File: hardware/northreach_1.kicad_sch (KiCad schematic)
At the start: 0 parts

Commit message: schematic: usb-c port section
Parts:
- added J1: USB_C_Receptacle, Connector_USB:USB_C_Receptacle_Amphenol_12401610E4-2A, symbol Connector:USB_C_Receptacle
- added R1, R2: 5.1k, Resistor_SMD:R_0805_2012Metric, symbol Device:R
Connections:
- new net: J1.A5 (CC1), R1.1
- new net: J1.B5 (CC2), R2.1
- new net GND: J1.A1 (GND), J1.A12 (GND), J1.B1 (GND), J1.B12 (GND), J1.S1 (SHIELD), R1.2, R2.2
- new net USB_D_NEGATIVE: J1.A7 (D-), J1.B7 (D-)
- new net USB_D_POSITIVE: J1.A6 (D+), J1.B6 (D+)
- new net VBUS: J1.A4 (VBUS), J1.A9 (VBUS), J1.B4 (VBUS), J1.B9 (VBUS)
- no-connect marks 0 -> 10
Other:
- note added: "USB-C Port"

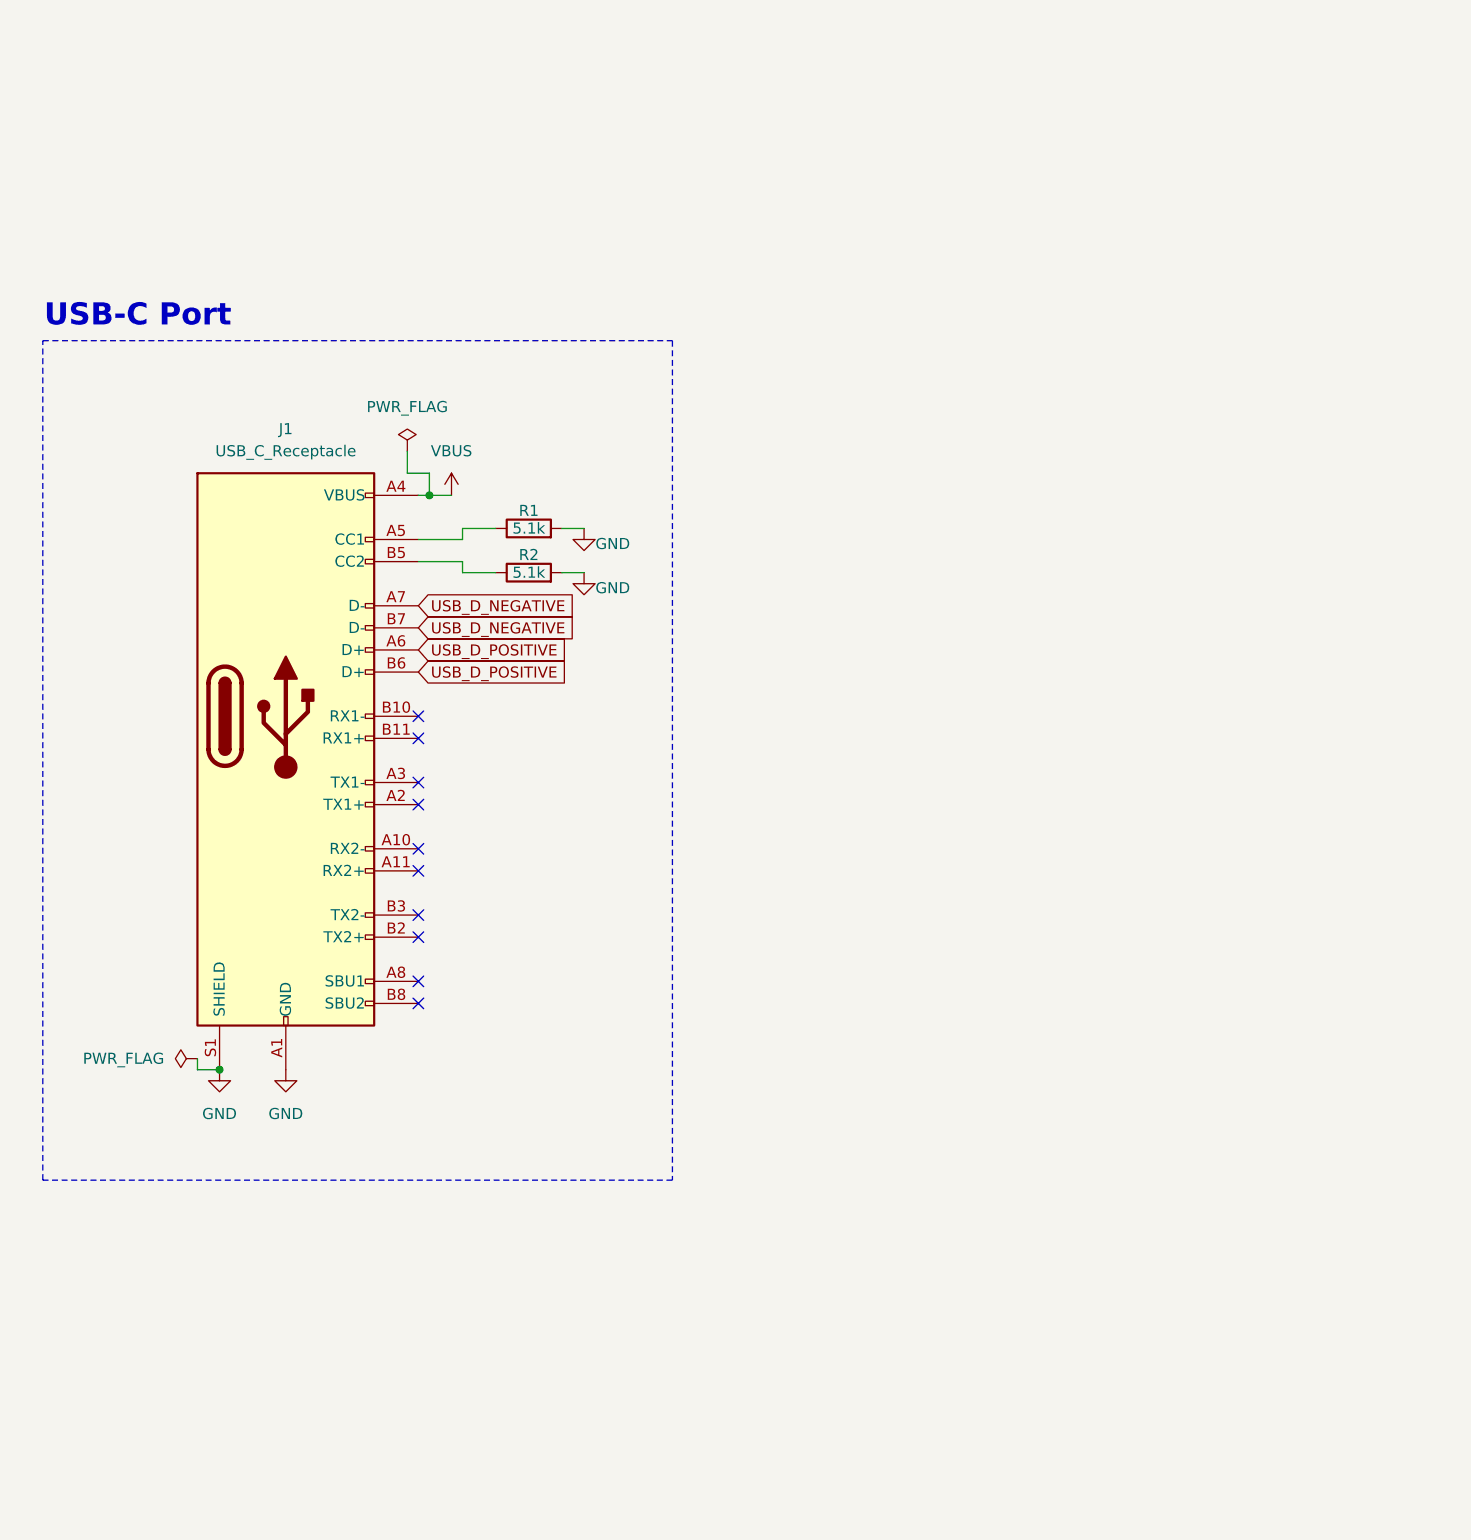
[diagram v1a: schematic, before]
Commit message: schematic: add voltage regulator
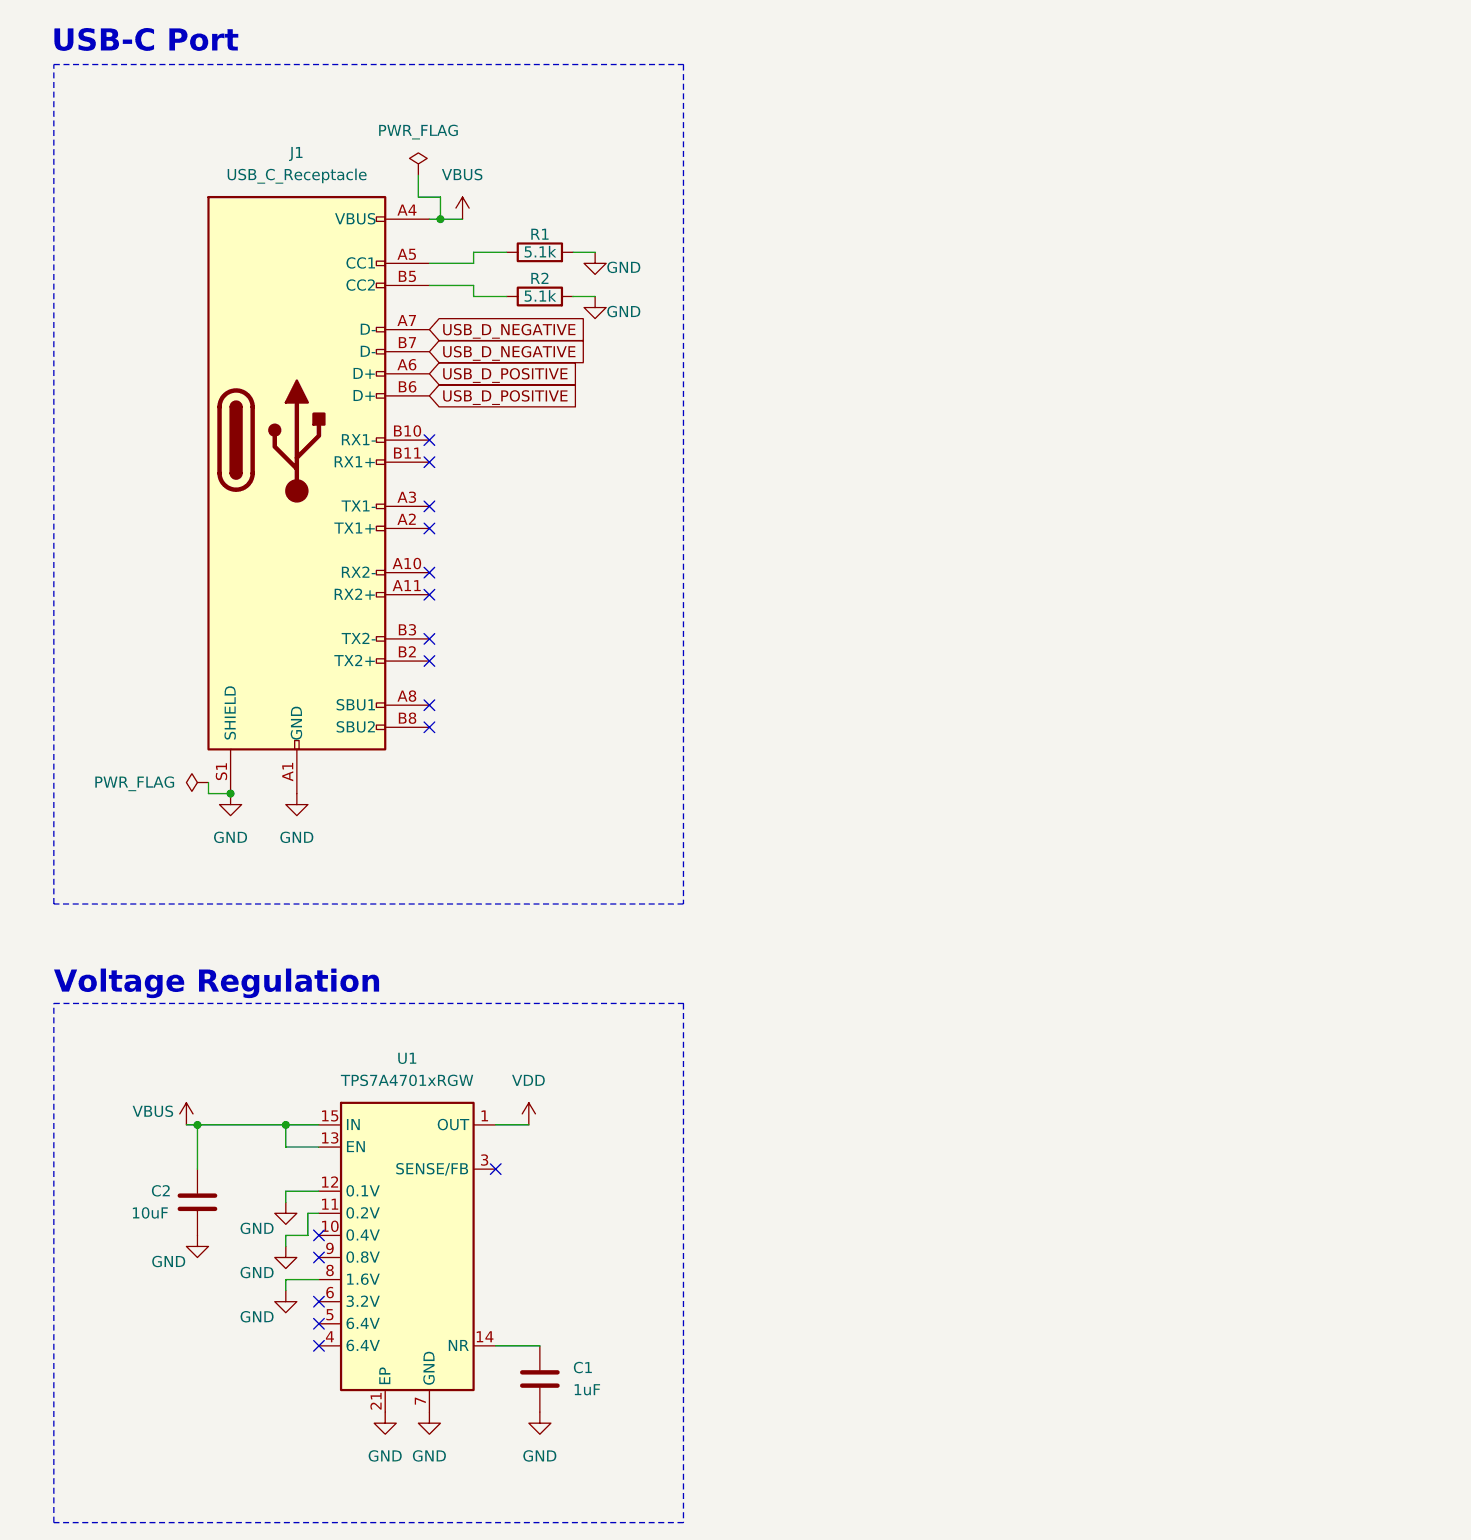
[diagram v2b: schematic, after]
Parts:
- added C1: 1uF, Capacitor_SMD:C_0805_2012Metric, symbol Device:C
- added C2: 10uF, Capacitor_SMD:C_0805_2012Metric, symbol Device:C
- added U1: TPS7A4701xRGW, Package_DFN_QFN:Texas_RGW0020A_VQFN-20-1EP_5x5mm_P0.65mm_EP3.15x3.15mm_ThermalVias, symbol Regulator_Linear:TPS7A4701xRGW
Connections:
- net GND: now also C1.1, C2.1, U1.11 (0.2V), U1.12 (0.1V), U1.21 (EP), U1.7 (GND), U1.8 (1.6V)
- net VBUS: now also C2.2, U1.13 (EN), U1.15 (IN), U1.16 (IN)
- new net: C1.2, U1.14 (NR)
- new net VDD: U1.1 (OUT), U1.20 (OUT)
- no-connect marks 10 -> 16
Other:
- note added: "Voltage Regulation"
- moved on the sheet: J1, R1, R2

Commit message: schematic: add MCU, and bootselect and reset buttons
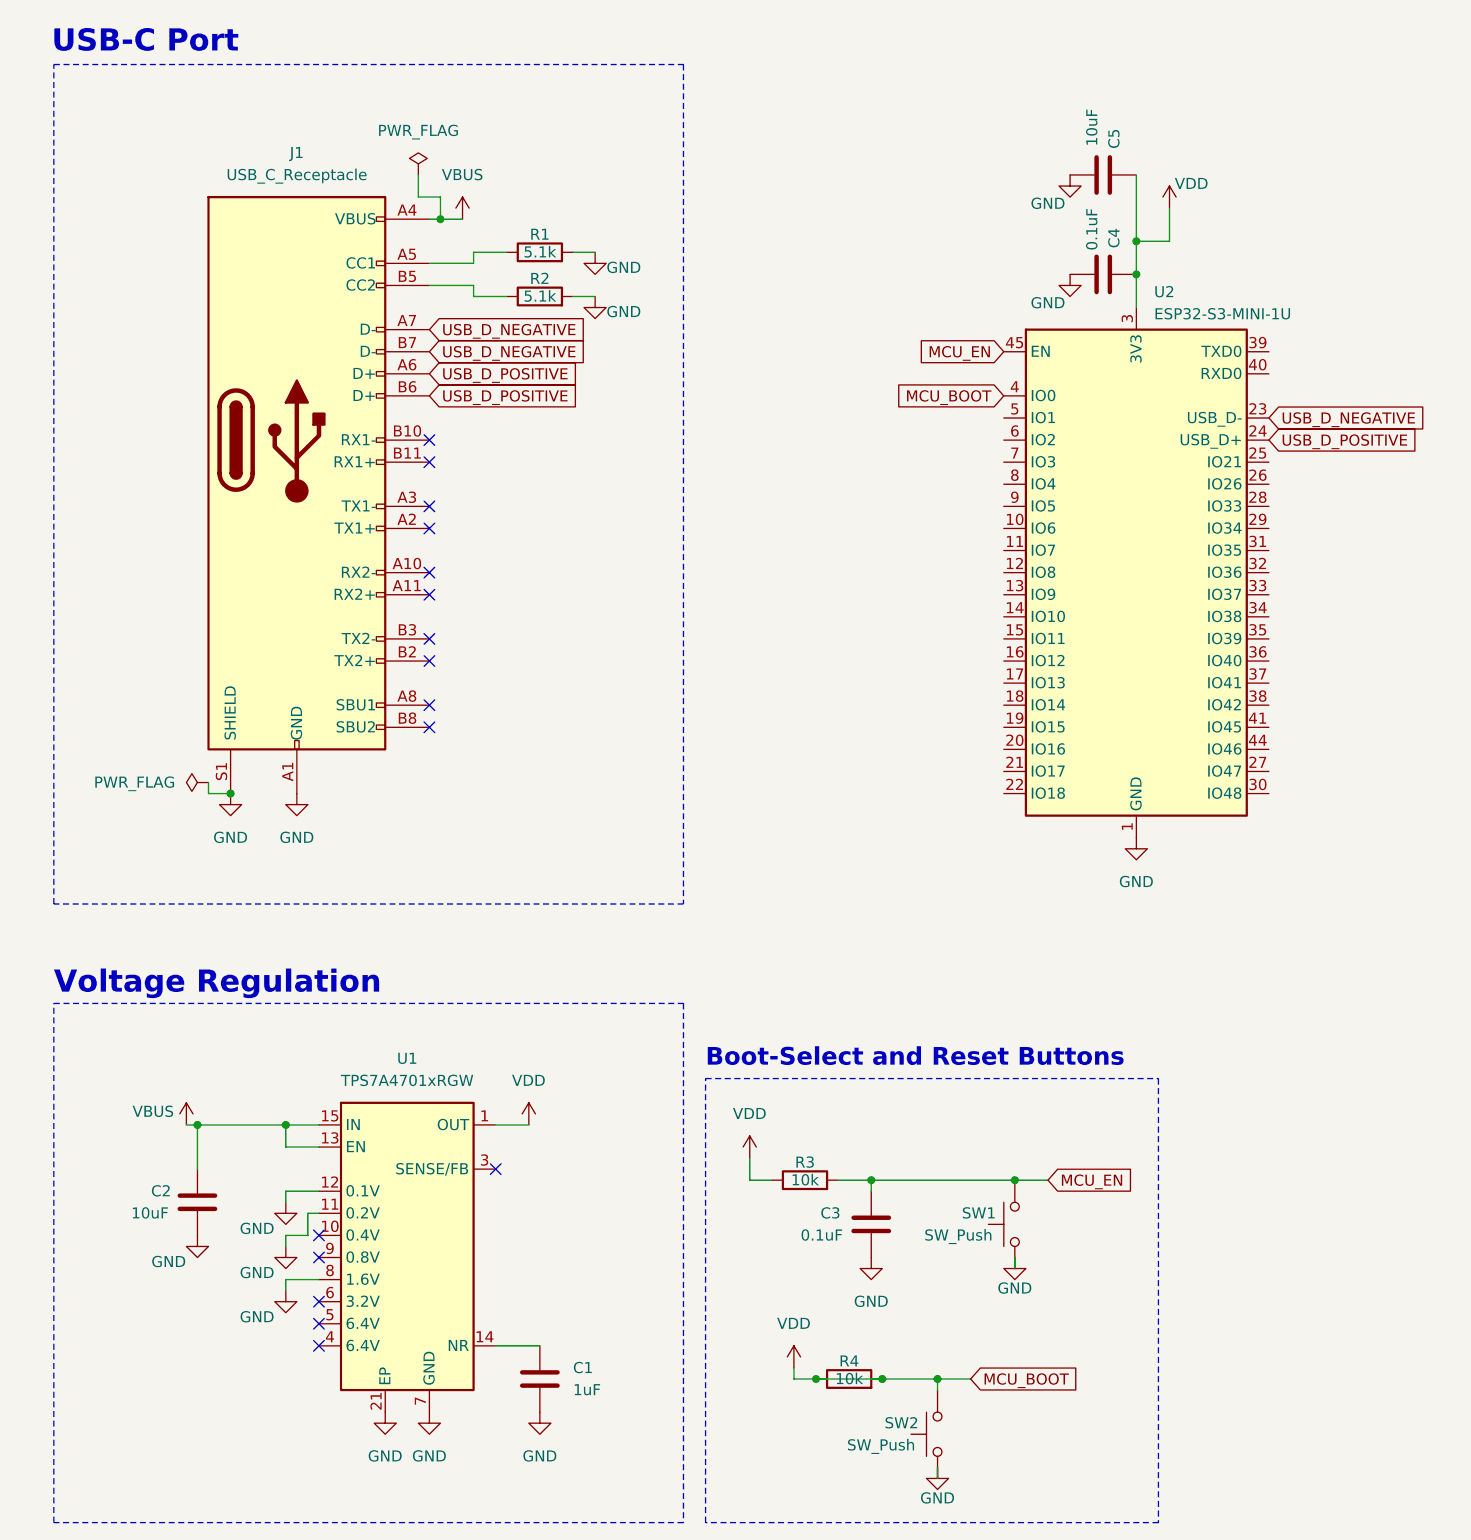
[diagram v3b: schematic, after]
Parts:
- added C3, C4: 0.1uF, Capacitor_SMD:C_0805_2012Metric, symbol Device:C
- added C5: 10uF, Capacitor_SMD:C_0805_2012Metric, symbol Device:C
- added R3, R4: 10k, Resistor_SMD:R_0805_2012Metric, symbol Device:R
- added SW1, SW2: SW_Push, Button_Switch_THT:SW_PUSH_6mm_H5mm, symbol Switch:SW_Push
- added U2: ESP32-S3-MINI-1U, RF_Module:ESP32-S2-MINI-1U, symbol RF_Module:ESP32-S3-MINI-1U
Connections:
- net GND: now also C3.1, C4.1, C5.1, SW1.1, SW2.1, U2.1 (GND), U2.2 (GND), U2.42 (GND), U2.43 (GND), U2.46 (GND), U2.47 (GND), U2.48 (GND), U2.49 (GND), U2.50 (GND), U2.51 (GND), U2.52 (GND), U2.53 (GND), U2.54 (GND), U2.55 (GND), U2.56 (GND), U2.57 (GND), U2.58 (GND), U2.59 (GND), U2.60 (GND), U2.61 (GND), U2.62 (GND), U2.63 (GND), U2.64 (GND), U2.65 (GND)
- net USB_D_NEGATIVE: now also U2.23 (USB_D-)
- net USB_D_POSITIVE: now also U2.24 (USB_D+)
- net VDD: now also C4.2, C5.2, R3.1, R4.1, R4.2, SW2.2, U2.3 (3V3), U2.4 (IO0)
- new net MCU_EN: C3.2, R3.2, SW1.2, U2.45 (EN)
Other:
- note added: "Boot-Select and Reset Buttons"

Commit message: schematic: MCU UART header
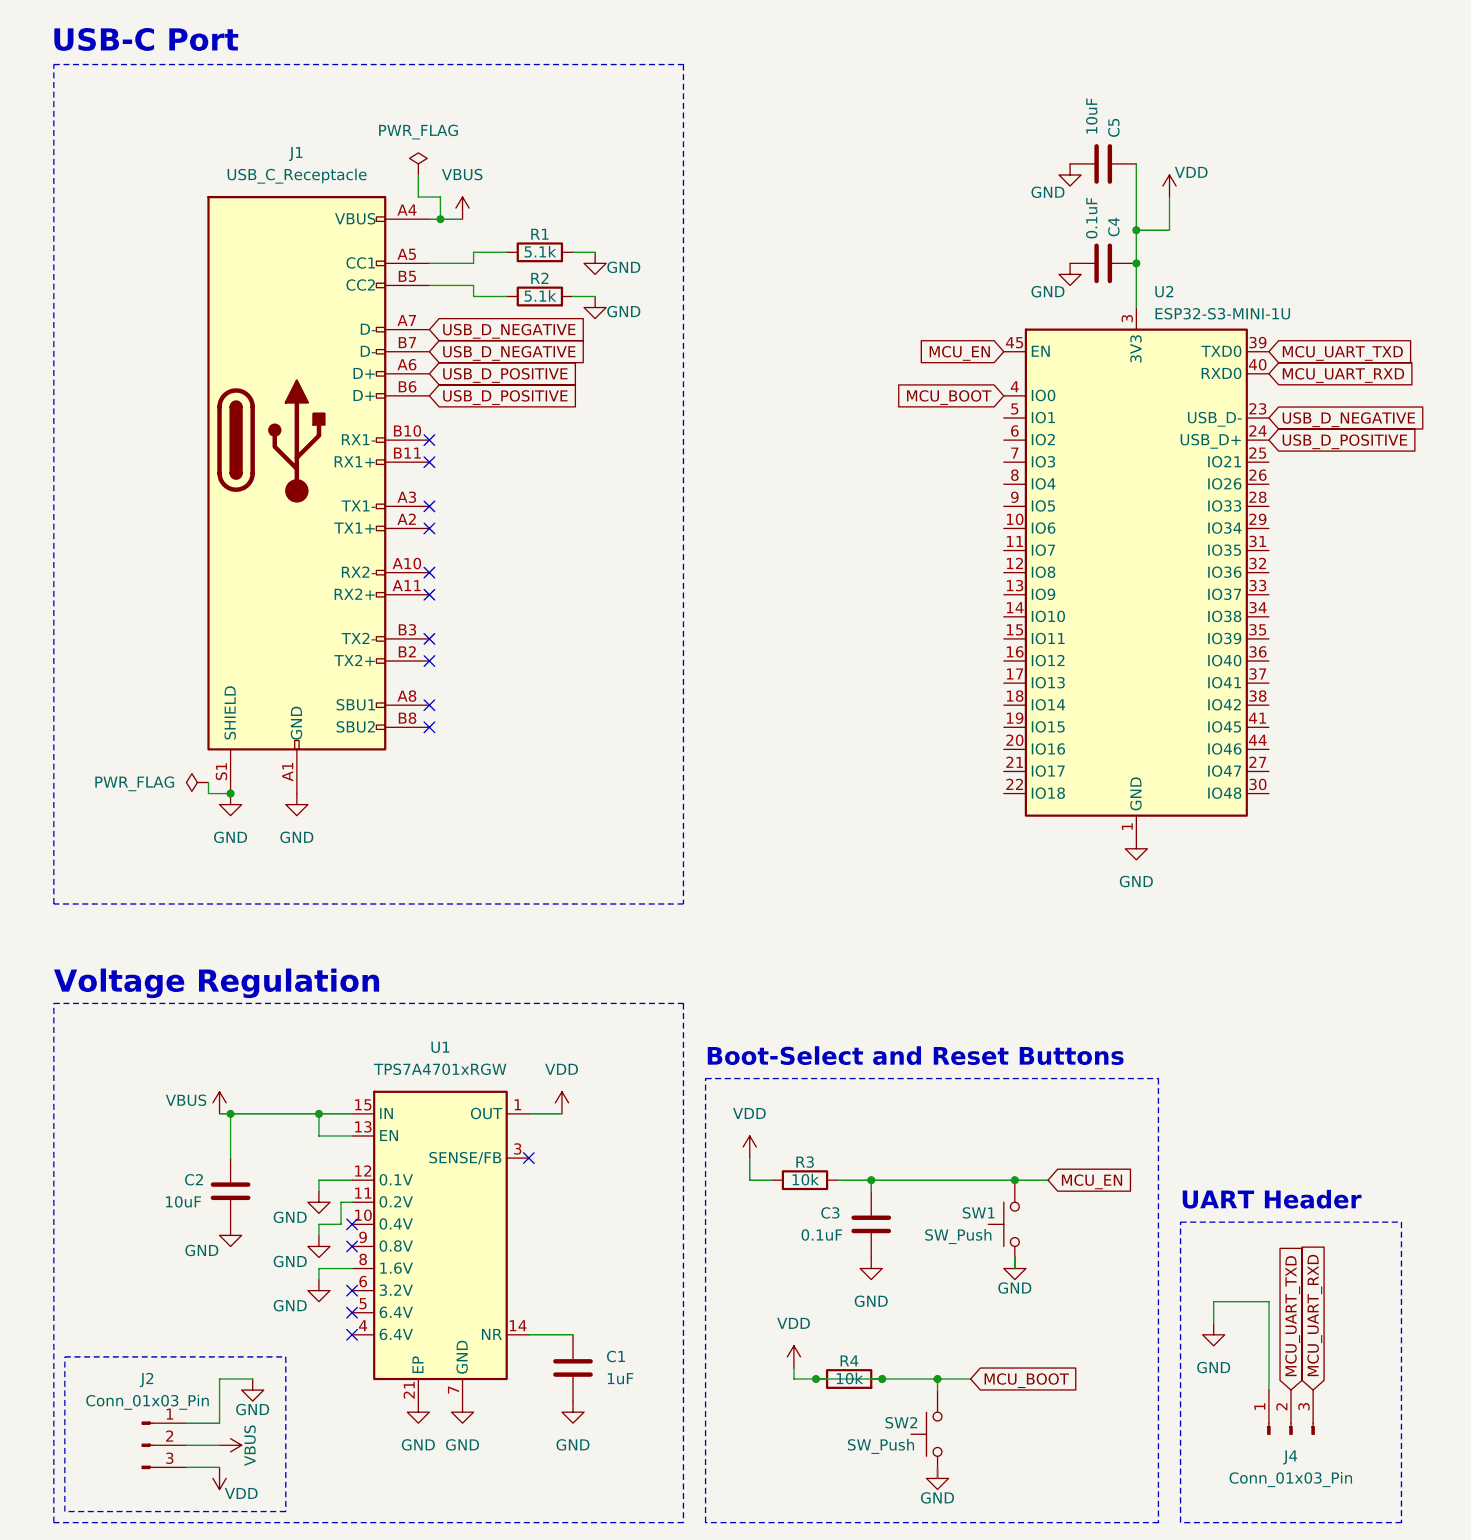
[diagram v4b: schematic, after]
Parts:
- added J2: Conn_01x03_Pin, Connector_PinHeader_2.54mm:PinHeader_1x03_P2.54mm_Vertical, symbol Connector:Conn_01x03_Pin
- added J4: Conn_01x03_Pin, symbol Connector:Conn_01x03_Pin
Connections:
- net GND: now also J2.1 (Pin_1), J4.1 (Pin_1)
- net VBUS: now also J2.2 (Pin_2)
- net VDD: now also J2.3 (Pin_3)
- net MCU_UART_TXD: now reaches U2.39 (TXD0)
- net MCU_UART_TXD: now also J4.2 (Pin_2)
- net MCU_UART_RXD: now reaches U2.40 (RXD0)
- net MCU_UART_RXD: now also J4.3 (Pin_3)
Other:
- note added: "UART Header"
- moved on the sheet: C1, C2, C4, C5, U1
